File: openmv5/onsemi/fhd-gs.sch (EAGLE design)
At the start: 54 parts, among them IC1 AR0135CS2C00SUEA0, IC2 TLV62568PDDCR, IC3 MIC5365-2.8YC5-TR, J1 DF12-36-DP, Q1 PMXB120EPEZ

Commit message: Finish out new onsemi cameras
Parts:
- added C31, C32, C33, C34, C35, C36, C37, C38: 0.22uF, rcl:C-EUC0201
- added C39, C41, C42, C43, C44, C46, C47, C48, C49: 4.7uF, 0402:CAP_0402
- added C40, C45, C50, C51: 22uF, SparkFun-Capacitors:22UF-0805-6.3V-20%
- added IC4: MIC5365-2.8YC5-TR, MIC5365-2.8YC5-TR:MIC5365-2.8YC5-TR
- added L7, L8, L9: 100, 0402:INDUCTOR_0402
- added R5: 100K, rcl:R-US_R0402
- C11, C21, C27, C28: value 4.7uF -> 0.22uF; device 0402:CAP_0402 -> rcl:C-EUC0201; MPN JMK105BBJ475MV-F -> GRM033R60J224ME15D
- C12, C2: value 22uF -> 4.7uF; device SparkFun-Capacitors:22UF-0805-6.3V-20% -> 0402:CAP_0402; MPN CL21A226MQQNNNE -> JMK105BBJ475MV-F
- C13, C3, C4: value 0.22uF -> 22uF; device rcl:C-EUC0201 -> SparkFun-Capacitors:22UF-0805-6.3V-20%; MPN GRM033R60J224ME15D -> CL21A226MQQNNNE
- C18: value 6.8pF -> 0.22uF; device 0402:CAP_0402 -> rcl:C-EUC0201; MPN GRM1555C1H6R8DA01D -> GRM033R60J224ME15D
- C20: value 0.22uF -> 6.8pF; device rcl:C-EUC0201 -> 0402:CAP_0402; MPN GRM033R60J224ME15D -> GRM1555C1H6R8DA01D
- C22, C29, C30: value 22uF -> 0.22uF; device SparkFun-Capacitors:22UF-0805-6.3V-20% -> rcl:C-EUC0201; MPN CL21A226MQQNNNE -> GRM033R60J224ME15D
- C24: value 4.7uF -> 22uF; device 0402:CAP_0402 -> SparkFun-Capacitors:22UF-0805-6.3V-20%; MPN JMK105BBJ475MV-F -> CL21A226MQQNNNE
- IC1: value AR0135CS2C00SUEA0 -> TLV62568PDDCR; device AR0135CS2C00SUEA0:AR0135CS2C00SUEA0 -> TLV62568PDDCR:TLV62568PDDCR; MPN AR0135CS2C00SUEA0-DRBR -> TLV62568PDDCR
- IC2: value TLV62568PDDCR -> AR0234CSSC00SUKA0; device TLV62568PDDCR:TLV62568PDDCR -> AR0234CSSC00SUKA0:AR0234CSSC00SUKA0; MPN TLV62568PDDCR -> (none)
- L3: value MAKK2016T2R2M -> 100; device MAKK2016T2R2M:MAKK2016T2R2M -> 0402:INDUCTOR_0402; MPN MAKK2016T2R2M -> MFBM1V1005-101-R
- L5: value 100 -> MAKK2016T2R2M; device 0402:INDUCTOR_0402 -> MAKK2016T2R2M:MAKK2016T2R2M; MPN MFBM1V1005-101-R -> MAKK2016T2R2M
- R1: value 200K -> 100K; MPN CRCW0402200KFKEDC -> AC0402FR-07100KL
- R4: value 100K -> 1.5K; MPN AC0402FR-07100KL -> RC0402FR-131K5L
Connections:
- removed net DCMI_D10: IC1.DOUT10, J1.24
- removed net DCMI_D11: IC1.DOUT11, J1.22
- removed net VDD_PLL: C11.2, C12.2, C3.1, IC1.VDD_PLL, L2.P$1
- new net CAP: C41.2, IC2.CAP_1UF_PHY
- new net RSVD: IC2.RSVD, R4.2
- new net VAA_PHY: C39.2, C40.2, C9.1, IC2.VAA_PHY, L6.P$1
- new net VDDIO_PHY: C11.1, C25.2, C26.2, IC2.VDDIO_PHY, L4.P$1
- new net VDDIO_PHY_REG: C46.2, IC1.EN, IC4.VOUT, L4.P$2
- new net VDD_DATA: C2.2, C22.1, C4.2, IC2.VDD_DATA, L2.P$1
- new net VDD_PHY: C10.1, C12.2, C13.2, IC2.VDD_PHY, L3.P$1
- net DCMI_CLK: now also IC2.EXTCLK; no longer IC1.EXTCLK
- net DCMI_D0: now also IC2.DOUT0, J1.9; no longer IC1.DOUT0, J1.3
- net DCMI_D1: now also IC2.DOUT1, J1.7; no longer IC1.DOUT1, J1.1
- net DCMI_D2: now also IC2.DOUT2, J1.31; no longer IC1.DOUT2, J1.9
- net DCMI_D3: now also IC2.DOUT3, J1.29; no longer IC1.DOUT3, J1.7
- net DCMI_D4: now also IC2.DOUT4, J1.35; no longer IC1.DOUT4, J1.31
- net DCMI_D5: now also IC2.DOUT5, J1.28; no longer IC1.DOUT5, J1.29
- net DCMI_D6: now also IC2.DOUT6, J1.26; no longer IC1.DOUT6, J1.35
- net DCMI_D7: now also IC2.DOUT7, J1.33; no longer IC1.DOUT7, J1.28
- net DCMI_D8: now also IC2.DOUT8, J1.24; no longer IC1.DOUT8, J1.26
- net DCMI_D9: now also IC2.DOUT9, J1.22; no longer IC1.DOUT9, J1.33
- net DCMI_FSIN: now also IC2.TRIGGER; no longer IC1.TRIGGER
- net DCMI_HSYNC: now also IC2.LINE_VALID; no longer IC1.LINE_VALID
- net DCMI_PCLK: now also IC2.PIXCLK; no longer IC1.PIXCLK
- net DCMI_PWDN_INT: now also R5.1; no longer R4.1
- net DCMI_SCL: now also IC2.SCLK; no longer IC1.SCLK
- net DCMI_SDA: now also IC2.SDATA; no longer IC1.SDATA
- net DCMI_VSYNC: now also IC2.FRAME_VALID; no longer IC1.FRAME_VALID
- net FB: now also C20.2, IC1.FB; no longer C18.2, IC2.FB
- net GND: now also C11.2, C13.1, C18.2, C21.2, C22.2, C27.2, C28.2, C29.2, C3.1, C30.2, C31.2, C32.2, C33.2, C34.2, C35.2, C36.2, C37.2, C38.2, C39.1, C4.1, C40.1, C41.1, C42.1, C43.1, C44.1, C45.1, C46.1, C47.1, C48.1, C49.1, C50.1, C51.1, IC1.GND, IC2.AGND0, IC2.AGND1, IC2.AGND2, IC2.AGND3, IC2.DGND0, IC2.DGND1, IC2.DGND10, IC2.DGND11, IC2.DGND12, IC2.DGND2, IC2.DGND3, IC2.DGND4, IC2.DGND5, IC2.DGND6, IC2.DGND7, IC2.DGND8, IC2.DGND9, IC2.GNDIO_PHY0, IC2.GNDIO_PHY1, IC2.OE_N, IC2.SADDR, IC2.TEST, IC4.GND, J1.1, J1.3, R4.1, R5.2; no longer C11.1, C13.2, C20.2, C21.1, C22.1, C27.1, C28.1, C29.1, C3.2, C30.1, C4.2, IC1.AGND0, IC1.AGND1, IC1.DGND0, IC1.DGND1, IC1.DGND2, IC1.DGND3, IC1.DGND4, IC1.DGND5, IC1.DGND6, IC1.OE_N, IC1.SADDR, IC1.STANDBY, IC1.TEST, IC2.GND, R4.2
- net RESET_N: now also IC1.PG, IC2.RESET_N; no longer IC1.RESET_N, IC2.PG
- net SPI_MISO: now also IC2.FLASH; no longer IC1.FLASH
- net SW: now also IC1.SW, L5.2; no longer IC2.SW, L3.2
- net VAA: now also C44.2, C45.2, C6.1, C7.1, C8.1, IC2.VAA0, IC2.VAA1, IC2.VAA2, IC2.VAA3, L7.P$1; no longer C25.2, C26.2, C4.1, IC1.VAA0, IC1.VAA1, L4.P$1
- net VAA_PIX: now also C27.1, C28.1, C29.1, C30.1, C48.2, C50.2, IC2.VAA_PIX0, IC2.VAA_PIX1, IC2.VAA_PIX2, IC2.VAA_PIX3, L8.P$1; no longer C13.1, C14.1, C27.2, C29.2, IC1.VAA_PIX0, IC1.VAA_PIX1, L5.P$1
- net VCC: now also C23.2, IC1.VIN; no longer C21.2, IC2.VIN
- net VDD: now also C14.1, C15.1, C16.1, C17.1, C18.1, C19.1, C21.1, C3.2, IC2.VDD0, IC2.VDD1, IC2.VDD2, IC2.VDD3, IC2.VDD4, IC2.VDD5, IC2.VDD6; no longer C10.1, C2.2, C6.1, C7.1, C8.1, C9.1, IC1.VDD0, IC1.VDD1, IC1.VDD2, IC1.VDD3, IC1.VDD4
- net VDDA: now also C43.2, C47.2, IC4.VIN; no longer C24.2
- net VDDIO: now also C31.1, C32.1, C33.1, C34.1, C35.1, C36.1, C37.1, C38.1, C49.2, C51.2, IC2.VDDIO0, IC2.VDDIO1, IC2.VDDIO2, IC2.VDDIO3, IC2.VDDIO4, IC2.VDDIO5, IC2.VDDIO6, IC2.VDDIO7, L9.P$1; no longer C15.1, C16.1, C17.1, C19.1, C20.1, C28.2, C30.2, IC1.VDDIO0, IC1.VDDIO1, IC1.VDDIO2, IC1.VDDIO3, IC1.VDDIO4, L6.P$1
- net VDDIO_REG: now also C42.2, IC4.EN, L7.P$2, L8.P$2, L9.P$2; no longer C23.2, IC2.EN, L2.P$2, L4.P$2, L5.P$2
- net VDD_REG: now also C20.1, C24.2, L2.P$2, L3.P$2, L5.1; no longer C18.1, C22.2, L3.1
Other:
- note added: "1.2V"
- moved on the sheet: C10, C11, C12, C13, C14, C15, C16, C17, C18, C19, C2, C20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

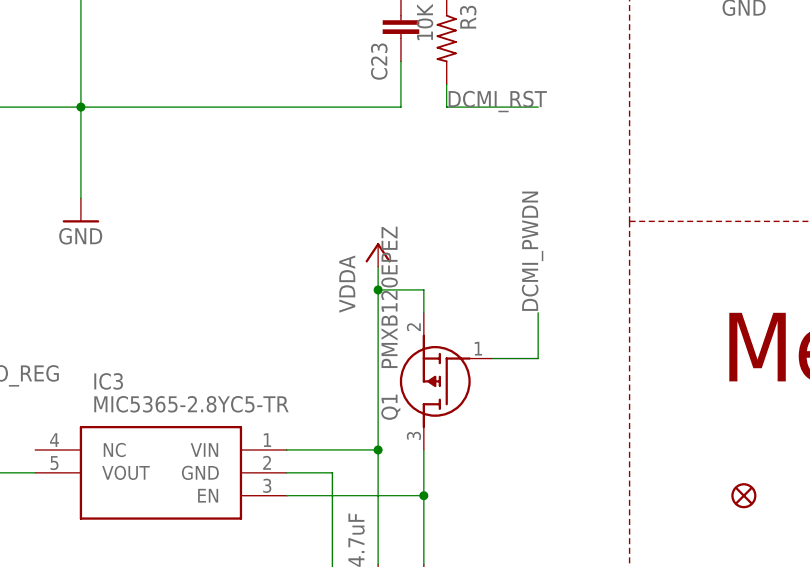
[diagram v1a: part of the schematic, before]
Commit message: Update camera modules to use different non-flippable pmosfet
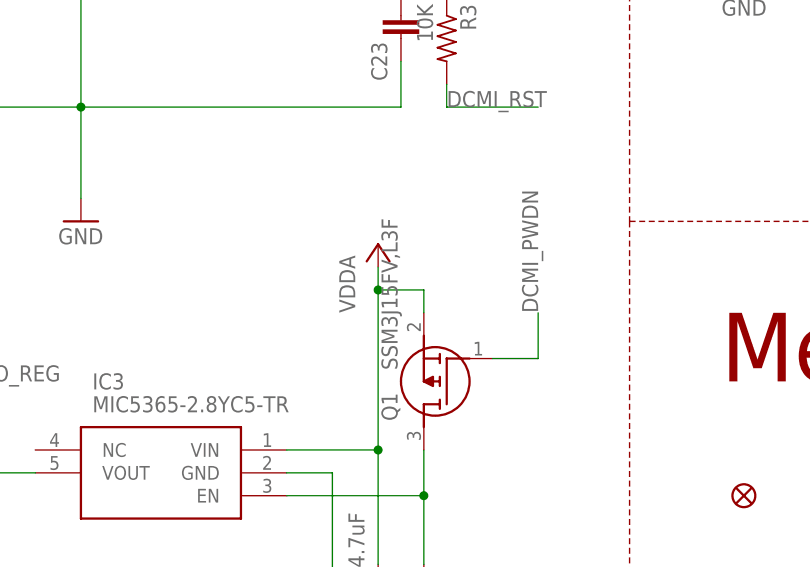
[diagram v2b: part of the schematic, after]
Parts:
- Q1: value PMXB120EPEZ -> SSM3J15FV,L3F; device PMXB120EPEZ:PMXB120EPEZ -> SSM3J15FV_L3F:SSM3J15FV,L3F; MPN PMXB120EPEZ -> SSM3J15FV,L3F
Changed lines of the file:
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@@
 </part>
 <part name="GND11" library="supply" deviceset="GND" device=""/>
-<part name="Q1" library="PMXB120EPEZ" deviceset="PMXB120EPEZ" device="">
-<attribute name="MPN" value="PMXB120EPEZ"/>
+<part name="Q1" library="SSM3J15FV_L3F" deviceset="SSM3J15FV,L3F" device="">
+<attribute name="MPN" value="SSM3J15FV,L3F"/>
 </part>
 <part name="R5" library="rcl" library_urn="urn:adsk.eagle:library:334" deviceset="R-US_" device="R0402" package3d_urn="urn:adsk.eagle:package:23547/3" value="100K">
